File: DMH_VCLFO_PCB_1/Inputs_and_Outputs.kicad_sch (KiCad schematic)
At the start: 49 parts, among them J1 TS_Jack_6.35mm_Sw, J10 IDC_02x05, J2 TS_Jack_6.35mm_Sw, J3 TS_Jack_6.35mm_Sw, J4 TS_Jack_6.35mm_Sw, J5 TS_Jack_6.35mm_Sw, J6 TS_Jack_6.35mm_Sw, SW1 SW_SPDT, SW2 SPDT_OnOffOn, SW3 SW_SPDT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

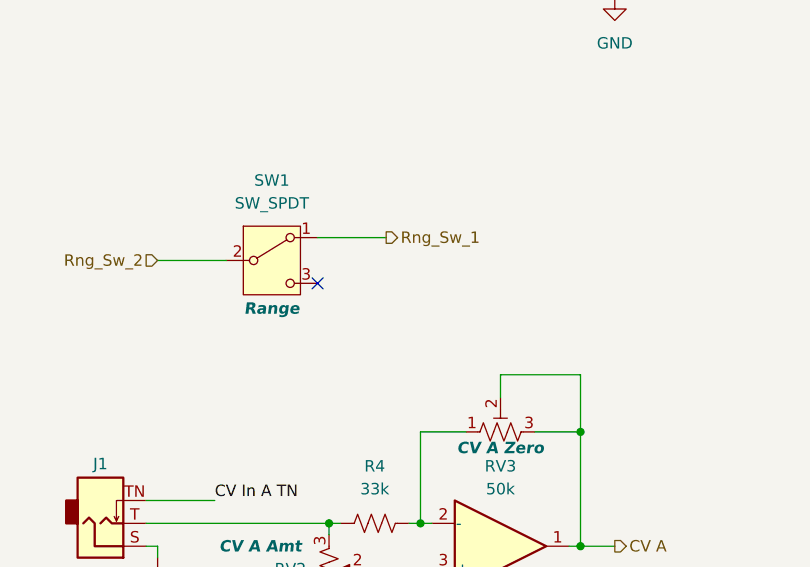
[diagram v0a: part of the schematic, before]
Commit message: Added super fast range option
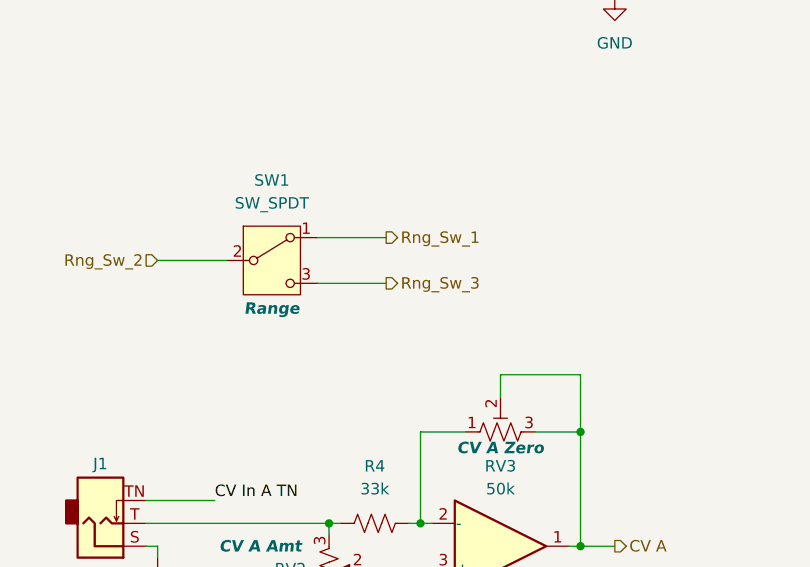
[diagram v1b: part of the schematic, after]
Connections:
- net Rng_Sw_3: now reaches SW1.3 (C)
- no-connect marks 1 -> 0
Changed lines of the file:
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@@
 		(color 0 0 0 0)
 	)
-	(no_connect
-		(at 49.53 72.39)
-	)
 	(wire
 		(pts
@@
 		(pts
 			(xy 148.59 231.14) (xy 152.4 231.14)
+		)
+		(stroke
+			(width 0)
+			(type default)
+		)
+	)
+	(wire
+		(pts
+			(xy 49.53 72.39) (xy 57.15 72.39)
 		)
 		(stroke
@@
 		)
 	)
+	(hierarchical_label "Rng_Sw_3"
+		(shape output)
+		(at 57.15 72.39 0)
+		(effects
+			(font
+				(size 1.27 1.27)
+			)
+			(justify left)
+		)
+	)
